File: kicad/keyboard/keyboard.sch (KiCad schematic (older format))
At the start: 132 parts, among them K0 KEYSW, K1 KEYSW, K10 KEYSW, K11 KEYSW, K12 KEYSW, K13 KEYSW, K14 KEYSW, K15 KEYSW, K16 KEYSW, K17 KEYSW, K18 KEYSW, K19 KEYSW, K2 KEYSW, K20 KEYSW, K21 KEYSW, K22 KEYSW, K23 KEYSW, K24 KEYSW, K25 KEYSW, K26 KEYSW, K27 KEYSW, K28 KEYSW, K29 KEYSW, K3 KEYSW, K30 KEYSW, K31 KEYSW, K32 KEYSW, K33 KEYSW, K34 KEYSW, K35 KEYSW, K36 KEYSW, K37 KEYSW, K38 KEYSW, K39 KEYSW, K4 KEYSW, K40 KEYSW, K41 KEYSW, K42 KEYSW, K43 KEYSW, K44 KEYSW, K45 KEYSW, K46 KEYSW, K47 KEYSW, K48 KEYSW, K49 KEYSW, K5 KEYSW, K50 KEYSW, K51 KEYSW, K52 KEYSW, K53 KEYSW, K54 KEYSW, K55 KEYSW, K56 KEYSW, K57 KEYSW, K58 KEYSW, K59 KEYSW, K6 KEYSW, K60 KEYSW, K61 KEYSW, K62 KEYSW, K63 KEYSW, K64 KEYSW, K65 KEYSW, K7 KEYSW, K9 KEYSW, U0 ProMicro, U1 74HC595

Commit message: added screw holes, positioned switches on pcb
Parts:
- K0, K1, K10, K11, K12, K13, K14, K15, K16, K17, K18, K19, K2, K20, K21, K22, K23, K24, K25, K26, K27, K28, K29, K3, K30, K31, K32, K33, K34, K35, K36, K37, K38, K39, K4, K40, K41, K42, K43, K44, K45, K46, K47, K48, K49, K5, K50, K51, K52, K53, K54, K55, K56, K57, K58, K59, K6, K60, K61, K62, K63, K64, K65, K7, K9: footprint Button_Switch_Keyboard:SW_Cherry_MX_1.00u_PCB -> kalih keyswitches:Kailh_socket

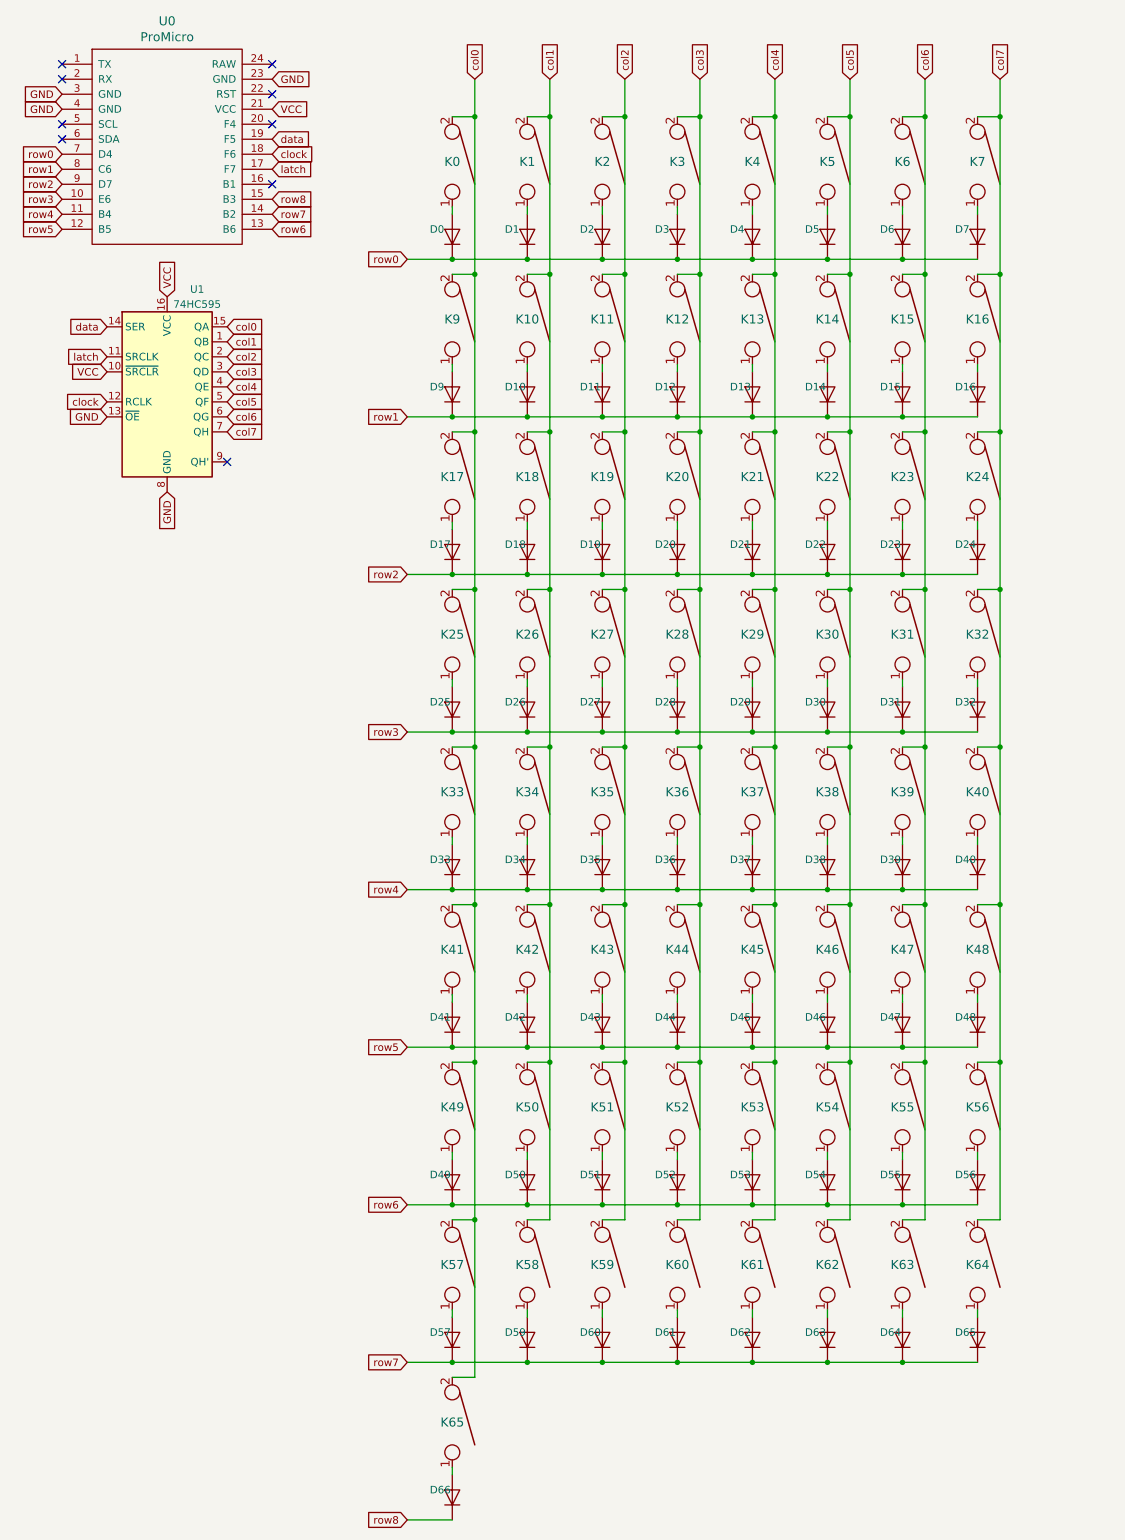
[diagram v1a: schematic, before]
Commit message: changed circuit to 5x13, designed pcb
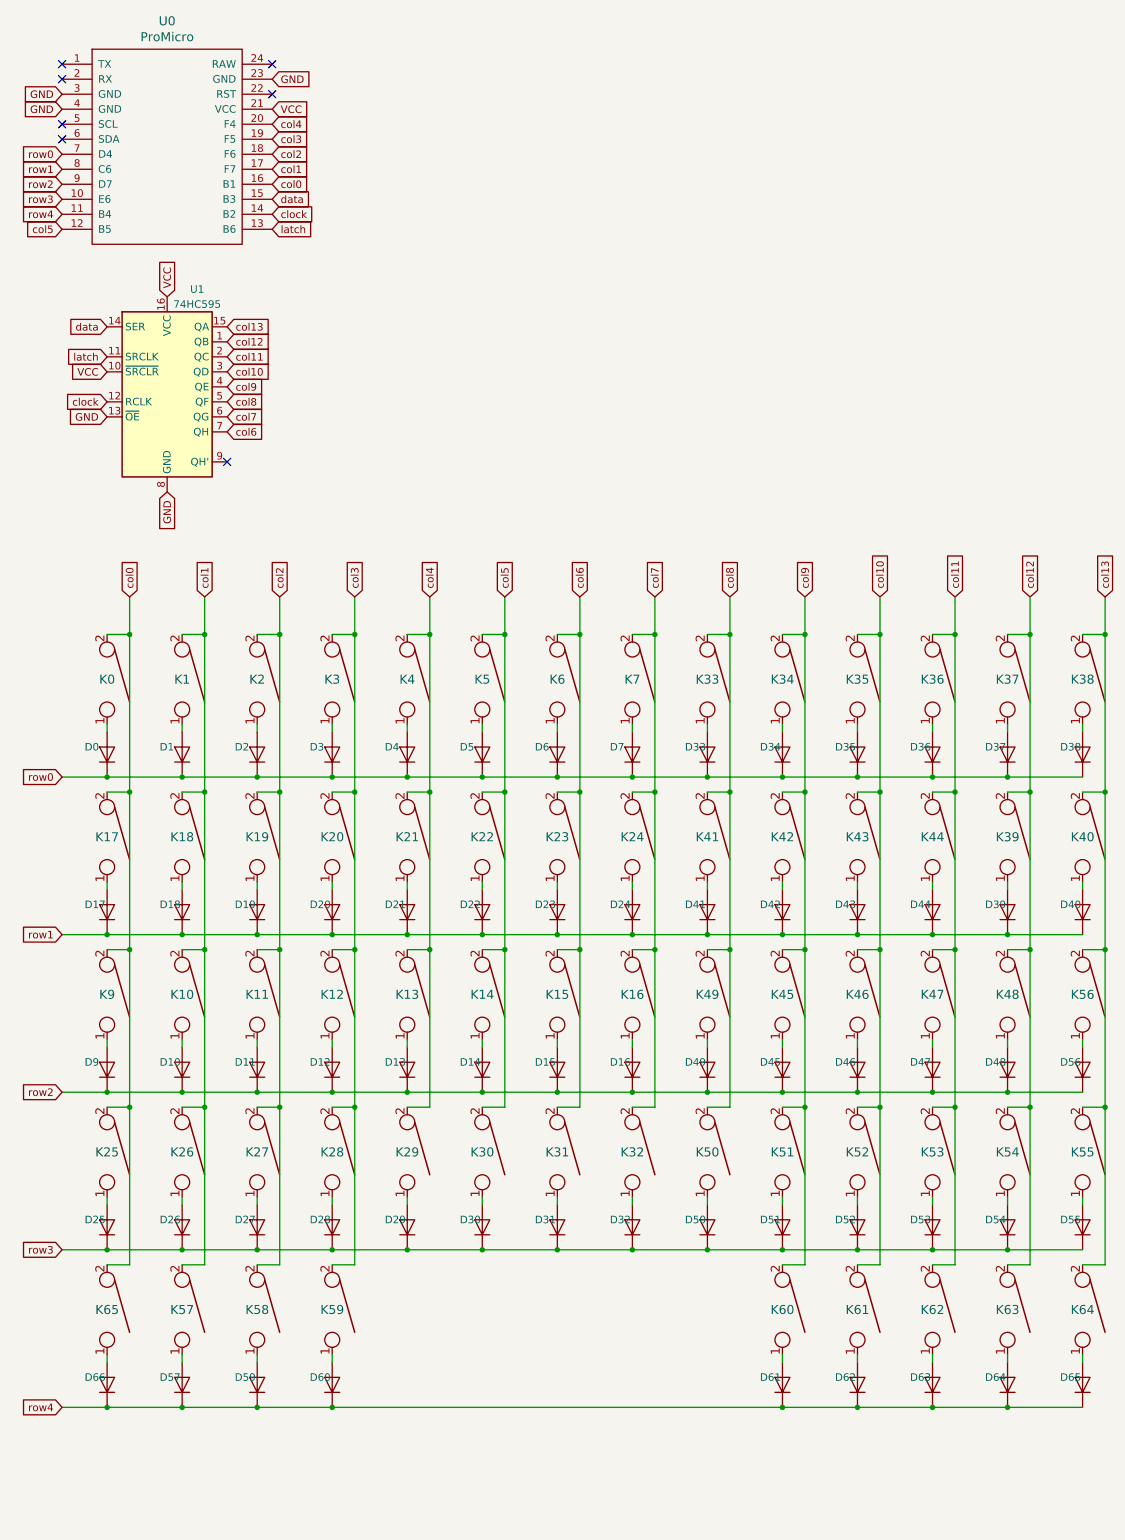
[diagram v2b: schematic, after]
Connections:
- net clock: now also U0.14 (B2); no longer U0.18 (F6)
- net col0: now also U0.16 (B1); no longer K33.2, K41.2, K49.2, K57.2, U1.15 (QA)
- net col1: now also K57.2, U0.17 (F7); no longer K34.2, K42.2, K50.2, K58.2, U1.1 (QB)
- net col2: now also K58.2, U0.18 (F6); no longer K35.2, K43.2, K51.2, K59.2, U1.2 (QC)
- net col3: now also K59.2, U0.19 (F5); no longer K36.2, K44.2, K52.2, K60.2, U1.3 (QD)
- net col4: now also U0.20 (F4); no longer K37.2, K45.2, K53.2, K61.2, U1.4 (QE)
- net col5: now also U0.12 (B5); no longer K38.2, K46.2, K54.2, K62.2, U1.5 (QF)
- net col6: now also U1.7 (QH); no longer K39.2, K47.2, K55.2, K63.2, U1.6 (QG)
- net col7: now also U1.6 (QG); no longer K40.2, K48.2, K56.2, K64.2, U1.7 (QH)
- net data: now also U0.15 (B3); no longer U0.19 (F5)
- net latch: now also U0.13 (B6); no longer U0.17 (F7)
- net row0: now also D33.1 (K), D34.1 (K), D35.1 (K), D36.1 (K), D37.1 (K), D38.1 (K)
- net row1: now also D17.1 (K), D18.1 (K), D19.1 (K), D20.1 (K), D21.1 (K), D22.1 (K), D23.1 (K), D24.1 (K), D39.1 (K), D40.1 (K), D41.1 (K), D42.1 (K), D43.1 (K), D44.1 (K); no longer D10.1 (K), D11.1 (K), D12.1 (K), D13.1 (K), D14.1 (K), D15.1 (K), D16.1 (K), D9.1 (K)
- net row2: now also D10.1 (K), D11.1 (K), D12.1 (K), D13.1 (K), D14.1 (K), D15.1 (K), D16.1 (K), D45.1 (K), D46.1 (K), D47.1 (K), D48.1 (K), D49.1 (K), D56.1 (K), D9.1 (K); no longer D17.1 (K), D18.1 (K), D19.1 (K), D20.1 (K), D21.1 (K), D22.1 (K), D23.1 (K), D24.1 (K)
- net row3: now also D50.1 (K), D51.1 (K), D52.1 (K), D53.1 (K), D54.1 (K), D55.1 (K)
- net row4: now also D57.1 (K), D59.1 (K), D60.1 (K), D61.1 (K), D62.1 (K), D63.1 (K), D64.1 (K), D65.1 (K), D66.1 (K); no longer D33.1 (K), D34.1 (K), D35.1 (K), D36.1 (K), D37.1 (K), D38.1 (K), D39.1 (K), D40.1 (K)
- removed net row5: D41.1 (K), D42.1 (K), D43.1 (K), D44.1 (K), D45.1 (K), D46.1 (K), D47.1 (K), D48.1 (K), U0.12 (B5)
- removed net row6: D49.1 (K), D50.1 (K), D51.1 (K), D52.1 (K), D53.1 (K), D54.1 (K), D55.1 (K), D56.1 (K), U0.13 (B6)
- removed net row7: D57.1 (K), D59.1 (K), D60.1 (K), D61.1 (K), D62.1 (K), D63.1 (K), D64.1 (K), D65.1 (K), U0.14 (B2)
- removed net row8: D66.1 (K), U0.15 (B3)
- new net col10: K35.2, K43.2, K46.2, K52.2, K61.2, U1.3 (QD)
- new net col11: K36.2, K44.2, K47.2, K53.2, K62.2, U1.2 (QC)
- new net col12: K37.2, K39.2, K48.2, K54.2, K63.2, U1.1 (QB)
- new net col13: K38.2, K40.2, K55.2, K56.2, K64.2, U1.15 (QA)
- new net col8: K33.2, K41.2, K49.2, K50.2, U1.5 (QF)
- new net col9: K34.2, K42.2, K45.2, K51.2, K60.2, U1.4 (QE)
- no-connect marks 9 -> 7
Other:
- moved on the sheet: D0, D1, D10, D11, D12, D13, D14, D15, D16, D17, D18, D19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

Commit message: flipped arduino to other side
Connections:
- net col2: now also U0.8 (C6); no longer U0.18 (F6)
- net col3: now also U0.10 (E6); no longer U0.19 (F5)
- net col4: now also U0.9 (D7); no longer U0.20 (F4)
- net data: now also U0.13 (B6); no longer U0.15 (B3)
- net latch: now also U0.15 (B3); no longer U0.13 (B6)
- net row0: now also U0.11 (B4); no longer U0.7 (D4)
- net row1: now also U0.20 (F4); no longer U0.8 (C6)
- net row2: now also U0.18 (F6); no longer U0.9 (D7)
- net row3: now also U0.19 (F5); no longer U0.10 (E6)
- net row4: now also U0.7 (D4); no longer U0.11 (B4)
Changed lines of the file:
@@
 	750  5650 1050 5650
 Connection ~ 1550 5650
-Text GLabel 2150 2000 2    50   Input ~ 0
-latch
 Text GLabel 2150 1900 2    50   Input ~ 0
 clock
-Text GLabel 2150 1800 2    50   Input ~ 0
+Text GLabel 2150 2000 2    50   Input ~ 0
 data
 Text GLabel 2150 1200 2    50   Input ~ 0
@@
 Text GLabel 3200 4450 1    50   Input ~ 0
 col4
+Text GLabel 750  1900 0    50   Input ~ 0
+row0
 Text GLabel 750  1500 0    50   Input ~ 0
-row0
-Text GLabel 750  1900 0    50   Input ~ 0
 row4
-Text GLabel 750  1600 0    50   Input ~ 0
+Text GLabel 2150 1300 2    50   Input ~ 0
 row1
-Text GLabel 750  1700 0    50   Input ~ 0
+Text GLabel 2150 1500 2    50   Input ~ 0
 row2
-Text GLabel 750  1800 0    50   Input ~ 0
+Text GLabel 2150 1400 2    50   Input ~ 0
 row3
 Text GLabel 750  5650 0    50   Input ~ 0
@@
 Text GLabel 750  2000 0    50   Input ~ 0
 col5
-Text GLabel 2150 1300 2    50   Input ~ 0
+Text GLabel 750  1700 0    50   Input ~ 0
 col4
-Text GLabel 2150 1400 2    50   Input ~ 0
+Text GLabel 750  1800 0    50   Input ~ 0
 col3
 Text GLabel 1850 3350 2    50   Input ~ 0
@@
 Text GLabel 2150 1600 2    50   Input ~ 0
 col1
-Text GLabel 2150 1500 2    50   Input ~ 0
+Text GLabel 750  1600 0    50   Input ~ 0
 col2
 Wire Wire Line
@@
 col10
 NoConn ~ 1850 3550
+Text GLabel 2150 1800 2    50   Input ~ 0
+latch
 $EndSCHEMATC
